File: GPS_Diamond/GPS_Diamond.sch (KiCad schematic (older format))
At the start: 27 parts, among them J1 CONN_01X04_MALE, J2 TEST_1P, J3 TEST_1P, J5 TEST_1P, J6 TEST_1P, U1 TCR2LE33LM, U2 STM32F042K6Ux

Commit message: Changed the boot0 jumper to a button and rearanged the baro.
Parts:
- B1: footprint jumper:SOLDER-JUMPER_1-WAY -> Buttons_Switches_SMD:SW_SPST_B3U-1000P
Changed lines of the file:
@@
 F 0 "B1" H 1900 2750 50  0000 L CNN
 F 1 "SW_Push" H 1850 2590 50  0000 C CNN
-F 2 "jumper:SOLDER-JUMPER_1-WAY" H 1850 2850 50  0001 C CNN
+F 2 "Buttons_Switches_SMD:SW_SPST_B3U-1000P" H 1850 2850 50  0001 C CNN
 F 3 "" H 1850 2850 50  0001 C CNN
 	1    1850 2650

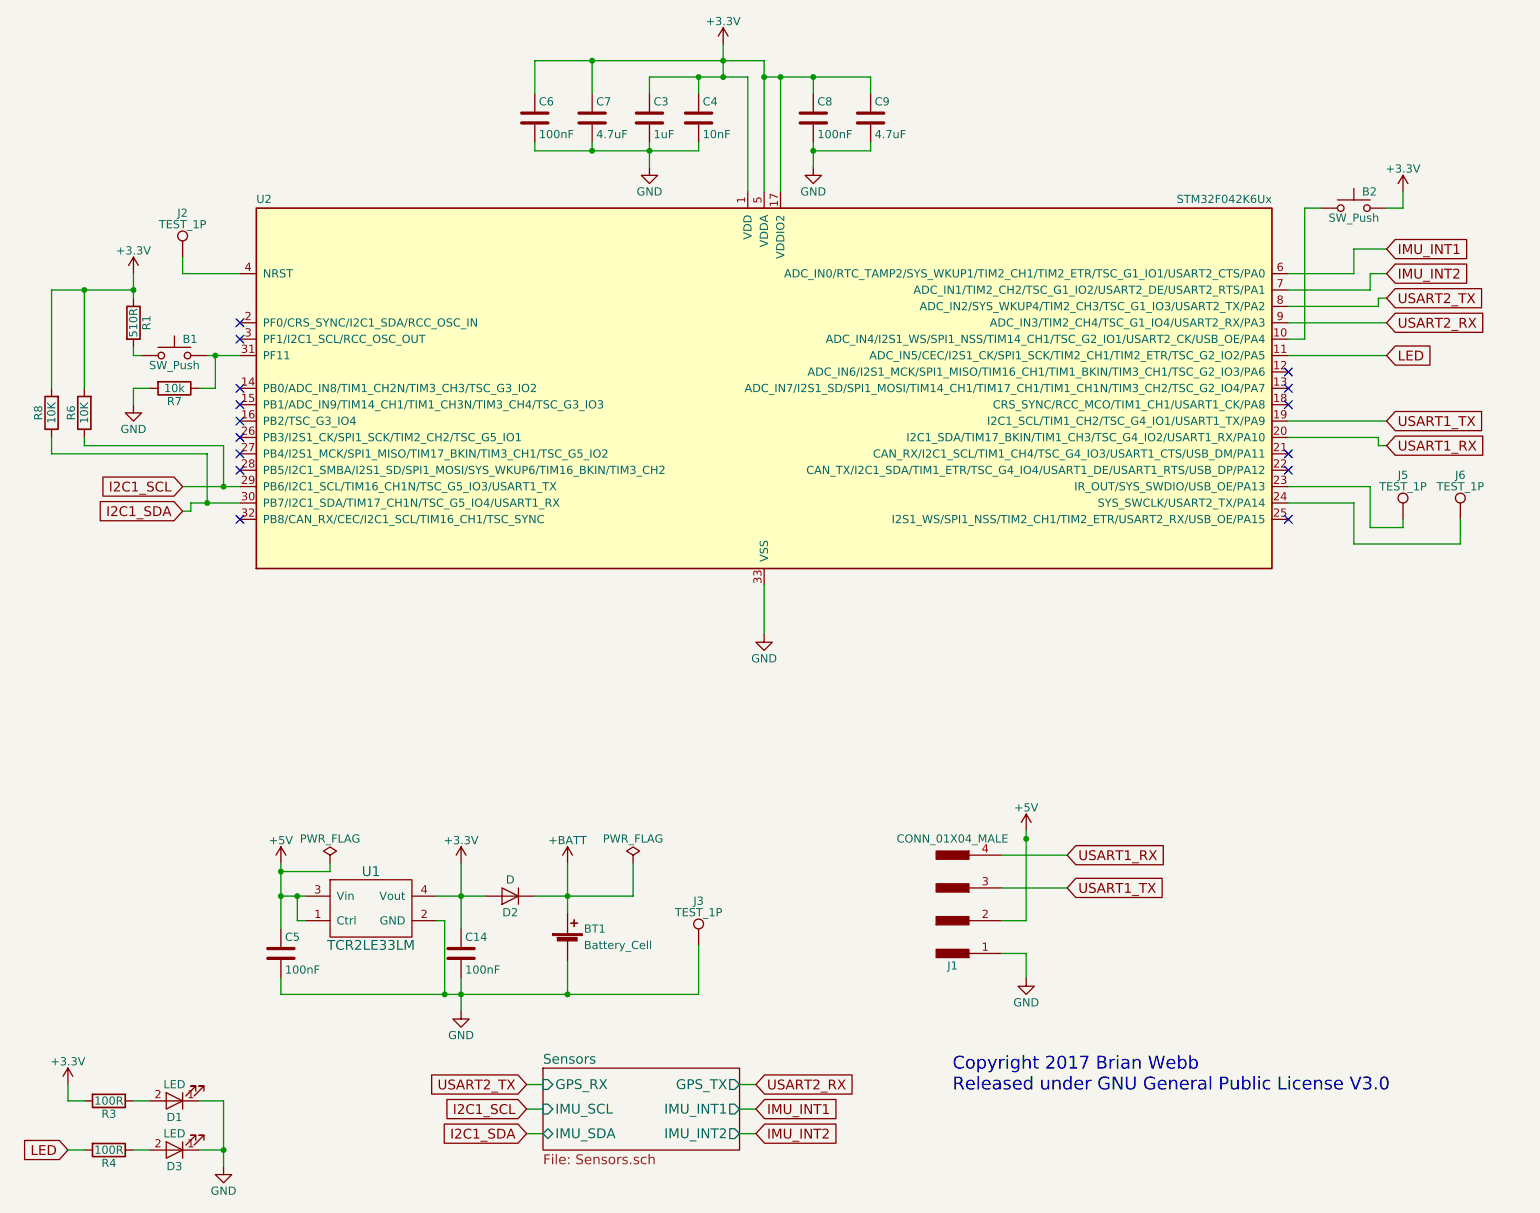
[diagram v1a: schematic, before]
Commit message: Updates GPS Diamond to 1.1.
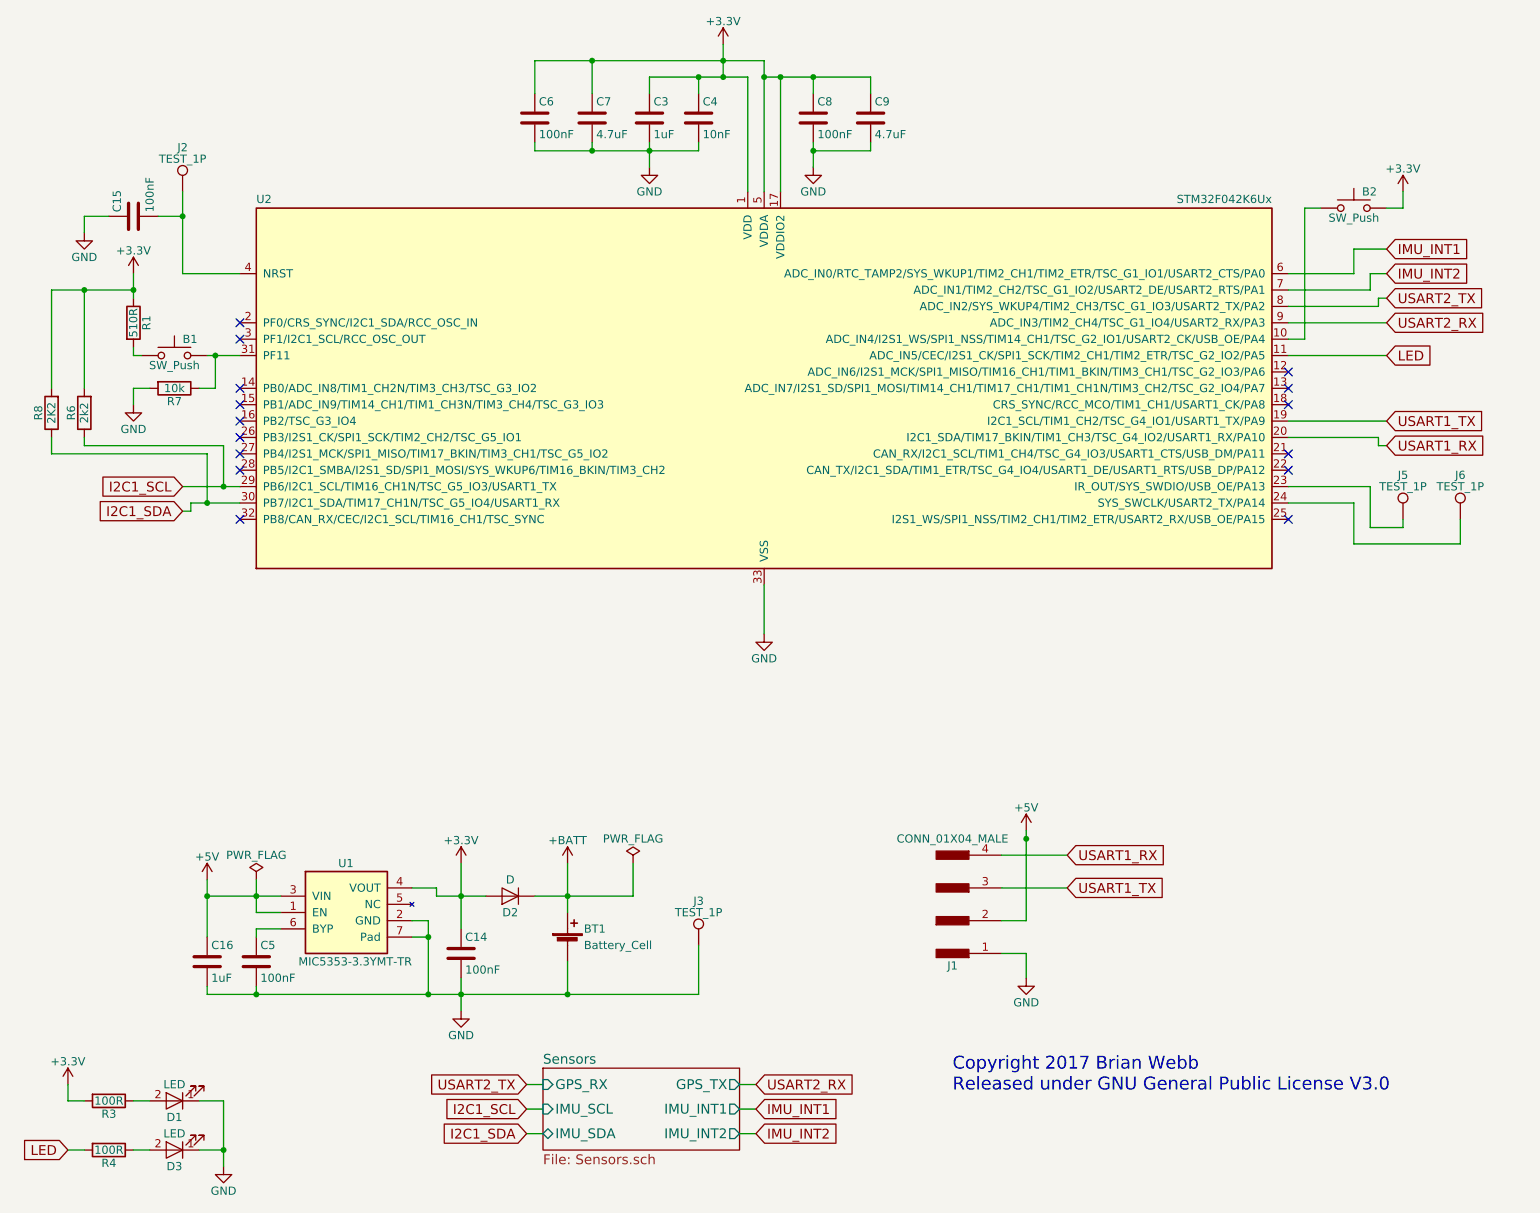
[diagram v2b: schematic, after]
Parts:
- removed U1: TCR2LE33LM, TO_SOT_Packages_SMD:SOT-553, symbol TCR2LE33LM
- added C15: 100nF, Capacitors_SMD:C_0402, symbol C
- added C16: 1uF, Capacitors_SMD:C_0402, symbol C
- added U1: MIC5353-3.3YMT-TR, local:MIC-5353, symbol MIC5353-3.3YMT-TR
- R6: value 10K -> 2k2
- R8: value 10K -> 2K2
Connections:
- net +3V3: now also U1.4 (VOUT)
- net +5V: now also C16.1, U1.1 (EN), U1.3 (VIN); no longer C5.1
- net GND: now also C15.1, C16.2, U1.2 (GND), U1.7 (Pad)
- net at J2.1, U2.4 (NRST): now also C15.2
- new net: C5.1, U1.6 (BYP)
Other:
- moved on the sheet: C5, J2
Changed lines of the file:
@@
 Sheet 1 2
 Title "GPS Diamond"
-Date "2017-04-29"
-Rev "1.0"
+Date "2017-06-07"
+Rev "1.1"
 Comp ""
 Comment1 ""
@@
 L +5V #PWR08
 U 1 1 58E699F2
-P 2500 5750
-F 0 "#PWR08" H 2500 5600 50  0001 C CNN
-F 1 "+5V" H 2500 5890 50  0000 C CNN
-F 2 "" H 2500 5750 50  0001 C CNN
-F 3 "" H 2500 5750 50  0001 C CNN
-	1    2500 5750
+P 2050 5850
+F 0 "#PWR08" H 2050 5700 50  0001 C CNN
+F 1 "+5V" H 2050 5990 50  0000 C CNN
+F 2 "" H 2050 5850 50  0001 C CNN
+F 3 "" H 2050 5850 50  0001 C CNN
+	1    2050 5850
 	1    0    0    -1
 $EndComp
@@
 L PWR_FLAG #FLG09
 U 1 1 58E69A7F
-P 2800 5750
-F 0 "#FLG09" H 2800 5825 50  0001 C CNN
-F 1 "PWR_FLAG" H 2800 5900 50  0000 C CNN
-F 2 "" H 2800 5750 50  0001 C CNN
-F 3 "" H 2800 5750 50  0001 C CNN
-	1    2800 5750
+P 2350 5850
+F 0 "#FLG09" H 2350 5925 50  0001 C CNN
+F 1 "PWR_FLAG" H 2350 6000 50  0000 C CNN
+F 2 "" H 2350 5850 50  0001 C CNN
+F 3 "" H 2350 5850 50  0001 C CNN
+	1    2350 5850
 	1    0    0    -1
 $EndComp
@@
 L TEST_1P J2
 U 1 1 58E881E3
-P 1900 2050
-F 0 "J2" H 1900 2320 50  0000 C CNN
-F 1 "TEST_1P" H 1900 2250 50  0000 C CNN
-F 2 "Measurement_Points:Measurement_Point_Square-SMD-Pad_Small" H 2100 2050 50  0001 C CNN
-F 3 "" H 2100 2050 50  0001 C CNN
-	1    1900 2050
+P 1900 1650
+F 0 "J2" H 1900 1920 50  0000 C CNN
+F 1 "TEST_1P" H 1900 1850 50  0000 C CNN
+F 2 "Measurement_Points:Measurement_Point_Square-SMD-Pad_Small" H 2100 1650 50  0001 C CNN
+F 3 "" H 2100 1650 50  0001 C CNN
+	1    1900 1650
 	1    0    0    -1
 $EndComp
@@
 L C C5
 U 1 1 59032334
-P 2500 6300
-F 0 "C5" H 2525 6400 50  0000 L CNN
-F 1 "100nF" H 2525 6200 50  0000 L CNN
-F 2 "Capacitors_SMD:C_0402" H 2538 6150 50  0001 C CNN
-F 3 "" H 2500 6300 50  0001 C CNN
-	1    2500 6300
+P 2350 6350
+F 0 "C5" H 2375 6450 50  0000 L CNN
+F 1 "100nF" H 2375 6250 50  0000 L CNN
+F 2 "Capacitors_SMD:C_0402" H 2388 6200 50  0001 C CNN
+F 3 "" H 2350 6350 50  0001 C CNN
+	1    2350 6350
 	1    0    0    -1
 $EndComp
@@
 	1900 2150 2250 2150
 Wire Wire Line
-	1900 2050 1900 2150
+	1900 1650 1900 2150
 Wire Wire Line
 	4050 850  4050 1050
@@
 	1    0    0    -1
 $EndComp
-Wire Wire Line
-	9250 1750 9350 1750
 Wire Wire Line
 	9350 1750 9350 1650
@@
 P 1100 3000
 F 0 "R8" V 1180 3000 50  0000 C CNN
-F 1 "10K" V 1100 3000 50  0000 C CNN
+F 1 "2K2" V 1100 3000 50  0000 C CNN
 F 2 "Resistors_SMD:R_0402" V 1030 3000 50  0001 C CNN
 F 3 "" H 1100 3000 50  0001 C CNN
@@
 P 1300 3000
 F 0 "R6" V 1380 3000 50  0000 C CNN
-F 1 "10K" V 1300 3000 50  0000 C CNN
+F 1 "2k2" V 1300 3000 50  0000 C CNN
 F 2 "Resistors_SMD:R_0402" V 1230 3000 50  0001 C CNN
 F 3 "" H 1300 3000 50  0001 C CNN
@@
 Wire Wire Line
 	8750 1750 8850 1750
-$Comp
-L TCR2LE33LM U1
-U 1 1 59049A29
-P 3050 6050
-F 0 "U1" H 3050 6300 60  0000 C CNN
-F 1 "TCR2LE33LM" H 3050 5850 60  0000 C CNN
-F 2 "TO_SOT_Packages_SMD:SOT-553" H 3000 5750 60  0001 C CNN
-F 3 "" H 3050 6050 60  0001 C CNN
-	1    3050 6050
-	1    0    0    -1
-$EndComp
 Wire Wire Line
 	4050 5950 4650 5950
 Wire Wire Line
 	3600 5750 3600 6150
-Wire Wire Line
-	2500 6550 5050 6550
 Wire Wire Line
 	3600 6450 3600 6650
 Connection ~ 3600 6550
-Wire Wire Line
-	2500 5950 2650 5950
-Wire Wire Line
-	2650 6100 2600 6100
-Wire Wire Line
-	2600 6100 2600 5950
-Connection ~ 2600 5950
-Wire Wire Line
-	2500 6450 2500 6550
-Wire Wire Line
-	3450 6100 3500 6100
-Wire Wire Line
-	3500 6100 3500 6550
-Connection ~ 3500 6550
 Wire Wire Line
 	5050 6550 5050 6250
@@
 IMU_INT2
 Wire Wire Line
-	3450 5950 3750 5950
-Connection ~ 3600 5950
-Wire Wire Line
 	2150 3450 2150 3200
 Wire Wire Line
@@
 Wire Wire Line
 	9050 3550 8650 3550
-Wire Wire Line
-	2500 5750 2500 6150
-Connection ~ 2500 5950
-Wire Wire Line
-	2800 5750 2800 5800
-Wire Wire Line
-	2800 5800 2500 5800
-Connection ~ 2500 5800
 $Comp
 L STM32F042K6Ux U2
@@
 	9250 2650 8650 2650
 NoConn ~ 2250 3650
+$Comp
+L C C15
+U 1 1 592C8166
+P 1600 1800
+F 0 "C15" H 1625 1900 50  0000 L CNN
+F 1 "100nF" H 1625 1700 50  0000 L CNN
+F 2 "Capacitors_SMD:C_0402" H 1638 1650 50  0001 C CNN
+F 3 "" H 1600 1800 50  0001 C CNN
+	1    1600 1800
+	0    -1   -1   0
+$EndComp
+Wire Wire Line
+	9250 1750 9350 1750
+$Comp
+L GND #PWR018
+U 1 1 592CA1DA
+P 1300 1900
+F 0 "#PWR018" H 1300 1650 50  0001 C CNN
+F 1 "GND" H 1300 1750 50  0000 C CNN
+F 2 "" H 1300 1900 50  0001 C CNN
+F 3 "" H 1300 1900 50  0001 C CNN
+	1    1300 1900
+	1    0    0    -1
+$EndComp
+Wire Wire Line
+	1750 1800 1900 1800
+Connection ~ 1900 1800
+Wire Wire Line
+	1450 1800 1300 1800
+Wire Wire Line
+	1300 1800 1300 1900
+Wire Wire Line
+	2050 6550 5050 6550
+Connection ~ 3600 5950
+Wire Wire Line
+	2350 6550 2350 6500
+Connection ~ 3400 6550
+$Comp
+L C C16
+U 1 1 5938AE1C
+P 2050 6350
+F 0 "C16" H 2075 6450 50  0000 L CNN
+F 1 "1uF" H 2075 6250 50  0000 L CNN
+F 2 "Capacitors_SMD:C_0402" H 2088 6200 50  0001 C CNN
+F 3 "" H 2050 6350 50  0001 C CNN
+	1    2050 6350
+	1    0    0    -1
+$EndComp
+Wire Wire Line
+	2050 6550 2050 6500
+Connection ~ 2350 6550
+Wire Wire Line
+	2050 5850 2050 6200
+$Comp
+L MIC5353-3.3YMT-TR U1
+U 1 1 5938C552
+P 2900 6050
+F 0 "U1" H 2850 6350 50  0000 L CNN
+F 1 "MIC5353-3.3YMT-TR" H 3300 5750 50  0000 R CNN
+F 2 "local:MIC-5353" H 2900 5650 50  0001 C CIN
+F 3 "" H 2900 6050 50  0000 C CNN
+	1    2900 6050
+	1    0    0    -1
+$EndComp
+Wire Wire Line
+	3300 5900 3450 5900
+Wire Wire Line
+	3450 5900 3450 5950
+Wire Wire Line
+	3450 5950 3750 5950
+Wire Wire Line
+	3400 6550 3400 6100
+Wire Wire Line
+	3400 6100 3300 6100
+Wire Wire Line
+	3300 6200 3400 6200
+Connection ~ 3400 6200
+Wire Wire Line
+	2500 5950 2050 5950
+Connection ~ 2050 5950
+Wire Wire Line
+	2350 5850 2350 6050
+Connection ~ 2350 5950
+Wire Wire Line
+	2350 6050 2500 6050
+Wire Wire Line
+	2500 6150 2350 6150
+Wire Wire Line
+	2350 6150 2350 6200
 $EndSCHEMATC

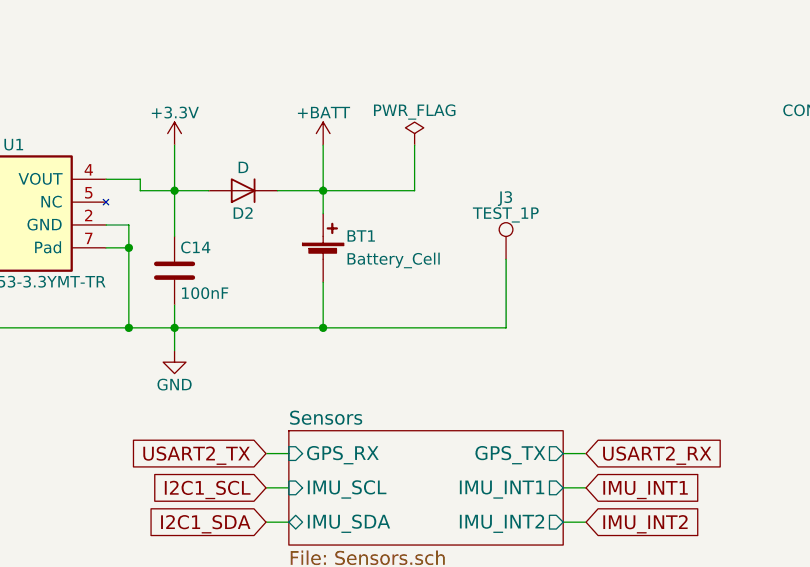
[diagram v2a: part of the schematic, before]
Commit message: GPS Diamond V1.1 working.
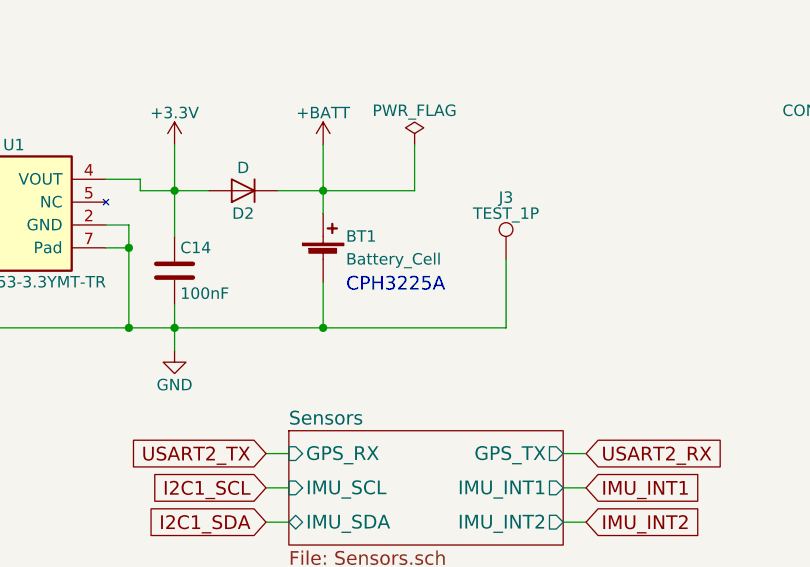
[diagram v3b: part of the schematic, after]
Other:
- note added: "CPH3225A"
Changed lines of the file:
@@
 Wire Wire Line
 	2350 6150 2350 6200
+Text Notes 4350 6400 0    60   ~ 0
+CPH3225A
 $EndSCHEMATC
